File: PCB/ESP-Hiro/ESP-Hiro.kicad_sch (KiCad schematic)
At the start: 117 parts, among them J1 CiKe2PinSock, J10 CiKe4pinSock, J10_1 CiKe4pinPlug, J11 CiKe4pinSock, J11_1 CiKe4pinPlug, J12 CiKe4pinSock, J12_1 CiKe4pinPlug, J13 CiKe4pinSock, J13_1 CiKe4pinPlug, J14 CiKe4pinSock, J14_1 CiKe4pinPlug, J15 CiKe4pinSock, J15_1 CiKe4pinPlug, J1_1 CiKe2PinPlug, J2 CiKe2PinSock, J2_1 CiKe2PinPlug, J3 CiKe2PinSock, J3_1 CiKe2PinPlug, J4 CiKe2PinSock, J4_1 CiKe2PinPlug, J5 CiKe2PinSock, J5_1 CiKe2PinPlug, J6 XUNPU TYPEC-304S-ACP16, J7 Barrel_Jack_Switch, J8 CiKe2PinSock, J8_1 CiKe2PinPlug, J9 CiKe4pinSock, J9_1 CiKe4pinPlug, Q1 AO3400A, Q2 AO3400A, Q3 AO3400A, Q4 AO3400A, Q5 AO3400A, Q6 S8050_correctpins, Q7 S8050_correctpins, U1 ESP-12E, U2 CP2102N-A01-GQFN28, U3 TPS54331D, U4 TLV75533PDBVR, U5 PCF8574APWR

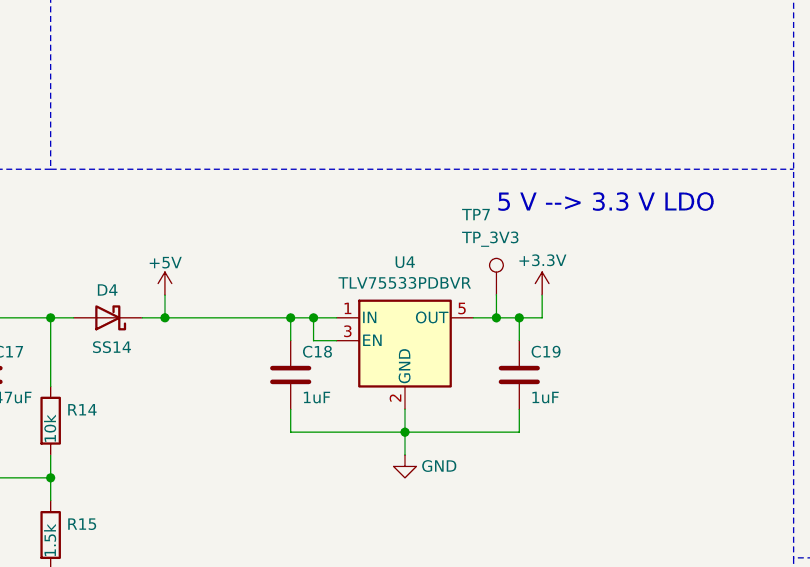
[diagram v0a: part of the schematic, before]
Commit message: Swap 3vV3 LDO to available part and order V1.0.1
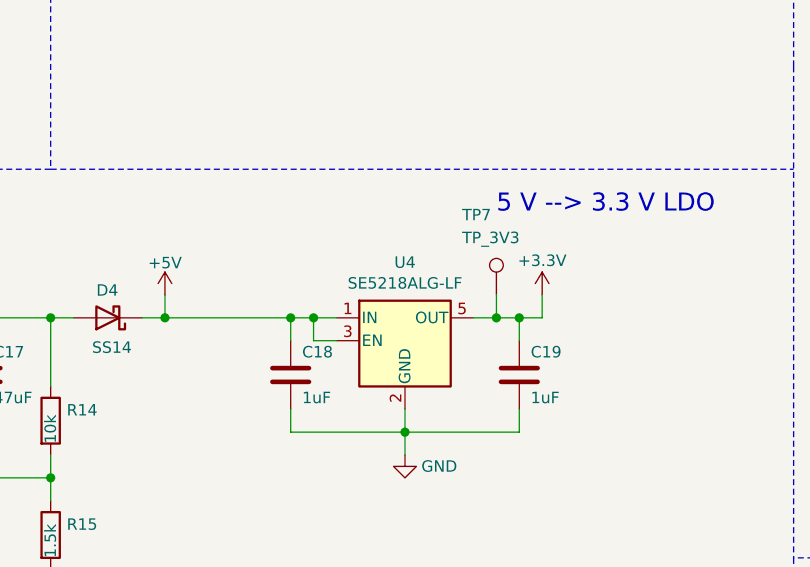
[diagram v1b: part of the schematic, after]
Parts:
- U4: value TLV75533PDBVR -> SE5218ALG-LF; LCSC C404027 -> C118233
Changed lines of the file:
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@@
     (in_bom yes) (on_board yes)
     (property "Reference" "U4" (id 0) (at 236.22 218.6432 0))
-    (property "Value" "TLV75533PDBVR" (id 1) (at 236.22 220.9546 0))
+    (property "Value" "SE5218ALG-LF" (id 1) (at 236.22 220.9546 0))
     (property "Footprint" "Package_TO_SOT_SMD:SOT-23-5" (id 2) (at 236.22 219.075 0)
       (effects (font (size 1.27 1.27) italic) hide)
     )
-    (property "Datasheet" "http://www.ti.com/lit/ds/symlink/tlv755p.pdf" (id 3) (at 236.22 226.06 0)
-      (effects (font (size 1.27 1.27)) hide)
-    )
-    (property "LCSC" "C404027" (id 4) (at 236.22 227.33 0)
+    (property "Datasheet" "https://datasheet.lcsc.com/lcsc/1810010120_Seaward-Elec-SE5218ALG-LF_C118233.pdf" (id 3) (at 236.22 226.06 0)
+      (effects (font (size 1.27 1.27)) hide)
+    )
+    (property "LCSC" "C118233" (id 4) (at 236.22 227.33 0)
       (effects (font (size 1.27 1.27)) hide)
     )
@@
     )
     (path "/00000000-0000-0000-0000-0000601a3a72"
-      (reference "U4") (unit 1) (value "TLV75533PDBVR") (footprint "Package_TO_SOT_SMD:SOT-23-5")
+      (reference "U4") (unit 1) (value "SE5218ALG-LF") (footprint "Package_TO_SOT_SMD:SOT-23-5")
     )
     (path "/494a5c65-fdb0-44ce-bf0e-cdc07b19a018"
